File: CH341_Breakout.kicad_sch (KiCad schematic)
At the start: 8 parts, among them J01 CONN_MODE, J11 CONN_I2C, J12 CONN_UART, J13 CONN_SPI, J21 CONN_SPI_FLASH, J22 CONN_I2C_EEPROM

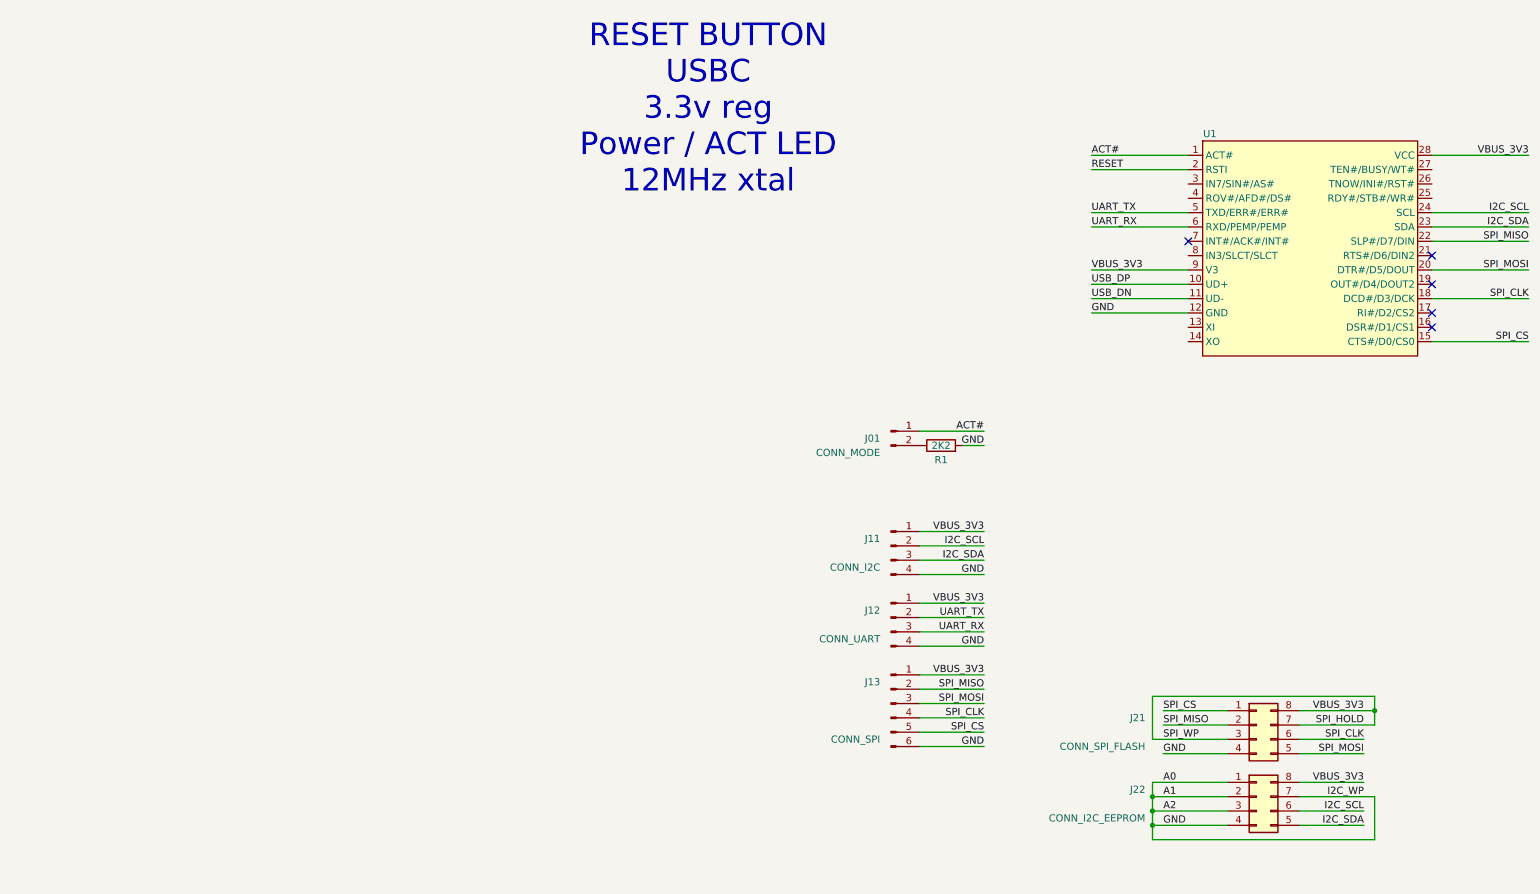
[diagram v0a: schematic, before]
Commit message: Added USB C and other bits
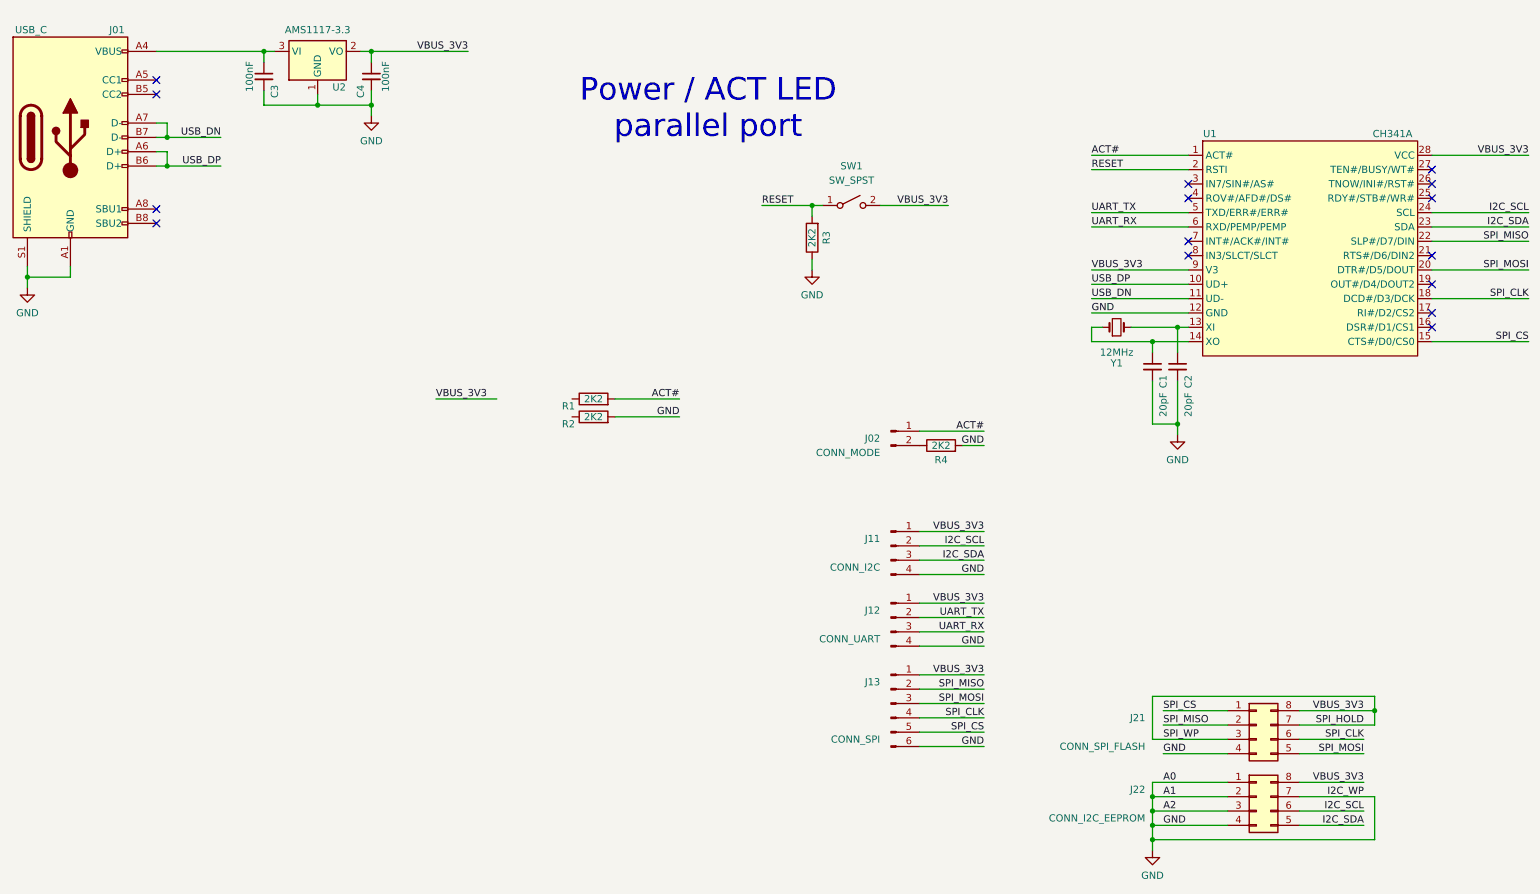
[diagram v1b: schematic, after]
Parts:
- added C1, C2: 20pF, Capacitor_SMD:C_0603_1608Metric, symbol Device:C_Small
- added C3, C4: 100nF, Capacitor_SMD:C_0603_1608Metric, symbol Device:C_Small
- added J01: USB_C, Connector_USB:USB_C_Receptacle_G-Switch_GT-USB-7010ASV, symbol Connector:USB_C_Receptacle_USB2.0_16P
- added R1, R2, R3: 2K2, Resistor_SMD:R_0603_1608Metric, symbol Device:R
- added SW1: SW_SPST, Button_Switch_SMD:SW_SPST_SKQG_WithoutStem, symbol Switch:SW_SPST
- added U2: AMS1117-3.3, Package_TO_SOT_SMD:SOT-223-3_TabPin2, symbol Regulator_Linear:AMS1117-3.3
- added Y1: 12MHz, symbol Device:Crystal_Small
- J21, J22: footprint (none) -> Connector_PinHeader_2.54mm:PinHeader_2x04_P2.54mm_Vertical
- R4: renamed from R1; footprint (none) -> Resistor_SMD:R_0603_1608Metric
- U1: value ~ -> CH341A; footprint (none) -> Package_SO:SOIC-28W_7.5x17.9mm_P1.27mm
- renumbered J01 to J02
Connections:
- net ACT#: now also R1.2
- net RESET: now also R3.2, SW1.1 (A)
- net SPI_HOLD: now also C4.1, SW1.2 (B), U2.2 (VO)
- net USB_DN: now also J01.A7 (D-), J01.B7 (D-)
- net USB_DP: now also J01.A6 (D+), J01.B6 (D+)
- net at U1.13 (XI): now also C2.1, Y1.2
- net at U1.14 (XO): now also C1.1, Y1.1
- net A0 renamed GND
- net GND: now also C1.2, C2.2, C3.2, C4.2, J01.A1 (GND), J01.A12 (GND), J01.B1 (GND), J01.B12 (GND), J01.S1 (SHIELD), R2.2, R3.1, U2.1 (GND)
- new net: C3.1, J01.A4 (VBUS), J01.A9 (VBUS), J01.B4 (VBUS), J01.B9 (VBUS), U2.3 (VI)
- no-connect marks 5 -> 15
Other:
- note added: "Power / ACT LED parallel port"
- note removed: "RESET BUTTON USBC 3.3v reg Power / ACT LED 12MHz xtal"
- company: (none) -> ADBeta
- title: (none) -> CH341A USB-C Breakout

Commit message: Started MkI PCB Design
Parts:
- removed C3: 100nF, Capacitor_SMD:C_0603_1608Metric, symbol Device:C_Small
- removed J11: CONN_I2C, Connector_PinHeader_2.54mm:PinHeader_1x04_P2.54mm_Vertical, symbol Connector:Conn_01x04_Pin
- removed J13: CONN_SPI, Connector_PinHeader_2.54mm:PinHeader_1x06_P2.54mm_Vertical, symbol Connector:Conn_01x06_Pin
- removed J21: CONN_SPI_FLASH, Connector_PinHeader_2.54mm:PinHeader_2x04_P2.54mm_Vertical, symbol Connector_Generic:Conn_02x04_Counter_Clockwise
- removed J22: CONN_I2C_EEPROM, Connector_PinHeader_2.54mm:PinHeader_2x04_P2.54mm_Vertical, symbol Connector_Generic:Conn_02x04_Counter_Clockwise
- added D1: ACT, LED_SMD:LED_0603_1608Metric, symbol Device:LED
- added D2: PWR, LED_SMD:LED_0603_1608Metric, symbol Device:LED
- added J12, J13: CONN_SPI_FLASH, symbol Connector_Generic:Conn_02x04_Odd_Even
- SW1: value SW_SPST -> RST
- Y1: footprint (none) -> Crystal:Crystal_HC49-U_Vertical
- renumbered C4 to C3, J12 to J11
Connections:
- net GND: now also J12.1 (Pin_1), J12.3 (Pin_3), J12.4 (Pin_4), J12.5 (Pin_5), J12.7 (Pin_7), J13.7 (Pin_7)
- net I2C_SCL: now also J12.6 (Pin_6)
- net I2C_SDA: now also J12.8 (Pin_8)
- net SPI_CS: now also J13.1 (Pin_1)
- net SPI_MISO: now also J13.3 (Pin_3)
- net SPI_MOSI: now also J13.8 (Pin_8)
- net at R2.1: now also D2.1 (K)
- net at R1.1: now also D1.1 (K)
- net SPI_CLK renamed SPI_SCLK
- net SPI_SCLK: now also J13.6 (Pin_6)
- net SPI_HOLD renamed VBUS_3V3
- net VBUS_3V3: now also D1.2 (A), D2.2 (A), J12.2 (Pin_2), J13.2 (Pin_2), J13.4 (Pin_4), J13.5 (Pin_5)
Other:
- note removed: "Power / ACT LED parallel port"
- moved on the sheet: J11, R1, R2, R3, SW1

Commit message: Finalised, built and tested
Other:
- moved on the sheet: C1, C2, C3, D1, D2, J01, J02, J11, J12, J13, R1, R2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
